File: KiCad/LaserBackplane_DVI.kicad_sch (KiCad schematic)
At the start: 45 parts, among them J1 Curr. Mod., J2 DVI-I, J3 Ld+, J4 Ld-, J5 Pz+, J6 Pz-, J7 Piezo_In, K1 G6AU, Q1 MMBT3904, Q2 2N4401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

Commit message: Add alternative part for inductor.
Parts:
- L1: Alternative (none) -> Coilcraft XAL5050-223MEC
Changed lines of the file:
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@@
+      (effects (font (size 1.27 1.27)) hide)
+    )
+    (property "Alternative" "Coilcraft XAL5050-223MEC" (id 6) (at 173.99 74.93 90)
       (effects (font (size 1.27 1.27)) hide)
     )

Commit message: Update document information
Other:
- company: APQ -> Atoms-Photons-Quanta, Institut für Angewandte Physik, TU Darmstadt
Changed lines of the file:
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@@
     (date "2021-12-16")
     (rev "1.7")
-    (company "APQ")
+    (company "Atoms-Photons-Quanta, Institut für Angewandte Physik, TU Darmstadt")
     (comment 1 "Tilman Preuschoff & Patrick Baus")
   )

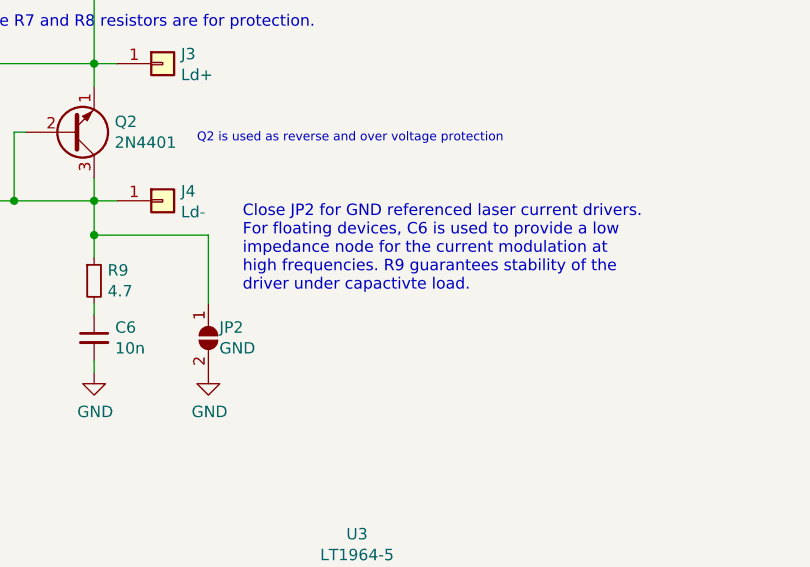
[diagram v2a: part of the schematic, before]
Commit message: Add variants ('default': without current mod., 'curr_mod': with current mod.)
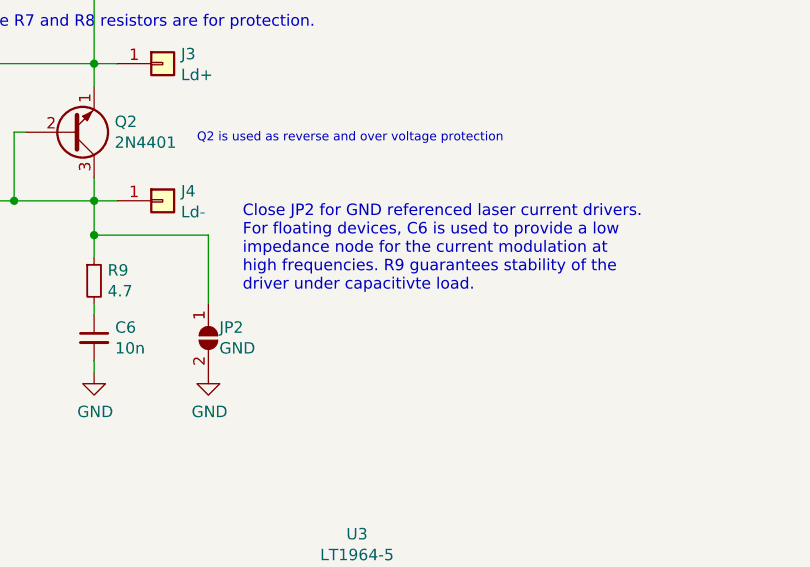
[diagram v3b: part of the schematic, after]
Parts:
- C10, C11, C12, C4, C7, C8, C9, R2, R4, R6, RN1, U1, U2, U3: Config (none) -> +curr_mod
- J1: Config DNF -> +curr_mod; MFN (none) -> Amphenol; PN (none) -> 132291
- J7: Config DNF -> (none); MFN (none) -> Amphenol; PN (none) -> 132291
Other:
- note added: "Close JP2 for GND referenced laser current drivers. For floating devices, C6 is used to provide a low impedance node for the current modulation at high frequencies. R9 guarantees stability of the driver under capacitivte load."
- note removed: "Close JP2 for GND referenced laser current drivers. For floating devices, C6 is used to provide a low impedance node for the current modulation at high frequencies. R9 guarantees stability of the driver under capactivte load."
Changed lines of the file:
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@@
   (title_block
     (title "Laser Backplane Diode DVI")
-    (date "2021-12-16")
-    (rev "1.7")
+    (date "2023-11-02")
+    (rev "1.7.2")
     (company "Atoms-Photons-Quanta, Institut für Angewandte Physik, TU Darmstadt")
     (comment 1 "Tilman Preuschoff & Patrick Baus")
@@
     (effects (font (size 1.524 1.524)) (justify left bottom))
   )
-  (text "Close JP2 for GND referenced laser current drivers. \nFor floating devices, C6 is used to provide a low\nimpedance node for the current modulation at \nhigh frequencies. R9 guarantees stability of the \ndriver under capactivte load."
+  (text "Close JP2 for GND referenced laser current drivers. \nFor floating devices, C6 is used to provide a low\nimpedance node for the current modulation at \nhigh frequencies. R9 guarantees stability of the \ndriver under capacitivte load."
     (at 229.87 107.95 0)
     (effects (font (size 1.27 1.27)) (justify left bottom))
@@
       (effects (font (size 1.27 1.27)) hide)
     )
-    (property "Config" "DNF" (id 4) (at 25.4 161.29 0)
+    (property "Config" "+curr_mod" (id 4) (at 25.4 161.29 0)
+      (effects (font (size 1.27 1.27)) hide)
+    )
+    (property "MFN" "Amphenol" (id 5) (at 25.4 161.29 0)
+      (effects (font (size 1.27 1.27)) hide)
+    )
+    (property "PN" "132291" (id 6) (at 25.4 161.29 0)
       (effects (font (size 1.27 1.27)) hide)
     )
@@
     )
     (property "PN" "RC1210FR-0749R9L" (id 5) (at 34.29 166.37 90)
+      (effects (font (size 1.27 1.27)) hide)
+    )
+    (property "Config" "+curr_mod" (id 6) (at 34.29 166.37 90)
       (effects (font (size 1.27 1.27)) hide)
     )
@@
       (effects (font (size 1.27 1.27)) hide)
     )
-    (property "Config" "DNF" (id 4) (at 257.81 29.21 0)
+    (property "Config" "" (id 4) (at 257.81 29.21 0)
+      (effects (font (size 1.27 1.27)) hide)
+    )
+    (property "MFN" "Amphenol" (id 5) (at 257.81 29.21 0)
+      (effects (font (size 1.27 1.27)) hide)
+    )
+    (property "PN" "132291" (id 6) (at 257.81 29.21 0)
       (effects (font (size 1.27 1.27)) hide)
     )
@@
       (effects (font (size 1.27 1.27)) hide)
     )
+    (property "Config" "+curr_mod" (id 6) (at 171.45 143.51 0)
+      (effects (font (size 1.27 1.27)) hide)
+    )
     (pin "1")
     (pin "2")
@@
       (effects (font (size 1.27 1.27)) hide)
     )
+    (property "Config" "+curr_mod" (id 6) (at 189.23 144.78 0)
+      (effects (font (size 1.27 1.27)) hide)
+    )
     (pin "1")
     (pin "2")
@@
       (effects (font (size 1.27 1.27)) hide)
     )
+    (property "Config" "+curr_mod" (id 6) (at 152.4 144.78 0)
+      (effects (font (size 1.27 1.27)) hide)
+    )
     (pin "1")
     (pin "2")
@@
     )
     (property "PN" "GRM21BR61H475KE51L" (id 5) (at 198.12 144.78 0)
+      (effects (font (size 1.27 1.27)) hide)
+    )
+    (property "Config" "+curr_mod" (id 6) (at 198.12 144.78 0)
       (effects (font (size 1.27 1.27)) hide)
     )
@@
       (effects (font (size 1.27 1.27)) hide)
     )
+    (property "Config" "+curr_mod" (id 6) (at 260.35 144.78 0)
+      (effects (font (size 1.27 1.27)) hide)
+    )
     (pin "1")
     (pin "2")
@@
       (effects (font (size 1.27 1.27)) hide)
     )
+    (property "Config" "+curr_mod" (id 6) (at 223.52 144.78 0)
+      (effects (font (size 1.27 1.27)) hide)
+    )
     (pin "1")
     (pin "2")
@@
     )
     (property "PN" "GRM21BR61H475KE51L" (id 5) (at 269.24 144.78 0)
+      (effects (font (size 1.27 1.27)) hide)
+    )
+    (property "Config" "+curr_mod" (id 6) (at 269.24 144.78 0)
       (effects (font (size 1.27 1.27)) hide)
     )
@@
       (effects (font (size 1.27 1.27)) hide)
     )
+    (property "Config" "+curr_mod" (id 6) (at 242.57 143.51 0)
+      (effects (font (size 1.27 1.27)) hide)
+    )
     (pin "1")
     (pin "2")
@@
       (effects (font (size 1.27 1.27)) hide)
     )
+    (property "Config" "+curr_mod" (id 6) (at 68.58 163.83 0)
+      (effects (font (size 1.27 1.27)) hide)
+    )
     (pin "1")
     (pin "2")
     (pin "3")
+    (pin "5")
+    (pin "6")
+    (pin "7")
+    (pin "4")
+    (pin "8")
   )
   (symbol (lib_id "Amplifier_Operational:ADA4807-2ARM") (at 113.03 166.37 0) (unit 2)
@@
       (effects (font (size 1.27 1.27)) hide)
     )
+    (property "Config" "+curr_mod" (id 6) (at 68.58 163.83 0)
+      (effects (font (size 1.27 1.27)) hide)
+    )
+    (pin "1")
+    (pin "2")
+    (pin "3")
     (pin "5")
     (pin "6")
     (pin "7")
+    (pin "4")
+    (pin "8")
   )
   (symbol (lib_id "Device:R_Pack04_Split") (at 90.17 163.83 270) (unit 1)
@@
       (effects (font (size 1.27 1.27)) hide)
     )
+    (property "Config" "+curr_mod" (id 6) (at 90.17 163.83 90)
+      (effects (font (size 1.27 1.27)) hide)
+    )
     (pin "1")
     (pin "8")
+    (pin "2")
+    (pin "7")
+    (pin "3")
+    (pin "6")
+    (pin "4")
+    (pin "5")
   )
   (symbol (lib_id "Device:R_Pack04_Split") (at 113.03 152.4 90) (mirror x) (unit 3)
@@
       (effects (font (size 1.27 1.27)) hide)
     )
+    (property "Config" "+curr_mod" (id 6) (at 90.17 163.83 90)
+      (effects (font (size 1.27 1.27)) hide)
+    )
+    (pin "1")
+    (pin "8")
+    (pin "2")
+    (pin "7")
     (pin "3")
     (pin "6")
+    (pin "4")
+    (pin "5")
   )
   (symbol (lib_id "Device:R_Pack04_Split") (at 113.03 179.07 90) (mirror x) (unit 4)
@@
       (effects (font (size 1.27 1.27)) hide)
     )
+    (property "Config" "+curr_mod" (id 6) (at 90.17 163.83 90)
+      (effects (font (size 1.27 1.27)) hide)
+    )
+    (pin "1")
+    (pin "8")
+    (pin "2")
+    (pin "7")
+    (pin "3")
+    (pin "6")
     (pin "4")
     (pin "5")
@@
       (effects (font (size 1.27 1.27)) hide)
     )
+    (property "Config" "+curr_mod" (id 6) (at 90.17 163.83 90)
+      (effects (font (size 1.27 1.27)) hide)
+    )
+    (pin "1")
+    (pin "8")
     (pin "2")
     (pin "7")
+    (pin "3")
+    (pin "6")
+    (pin "4")
+    (pin "5")
   )
   (symbol (lib_id "Device:C_Small") (at 113.03 187.96 270) (unit 1)
@@
       (effects (font (size 1.27 1.27)) hide)
     )
+    (property "Config" "+curr_mod" (id 6) (at 113.03 187.96 90)
+      (effects (font (size 1.27 1.27)) hide)
+    )
     (pin "1")
     (pin "2")
@@
       (effects (font (size 1.27 1.27)) hide)
     )
+    (property "Config" "+curr_mod" (id 6) (at 68.58 163.83 0)
+      (effects (font (size 1.27 1.27)) hide)
+    )
+    (pin "1")
+    (pin "2")
+    (pin "3")
+    (pin "5")
+    (pin "6")
+    (pin "7")
     (pin "4")
     (pin "8")
@@
       (effects (font (size 1.27 1.27)) hide)
     )
+    (property "Config" "+curr_mod" (id 6) (at 100.33 147.32 90)
+      (effects (font (size 1.27 1.27)) hide)
+    )
     (pin "1")
     (pin "2")
@@
       (effects (font (size 1.27 1.27)) hide)
     )
+    (property "Config" "+curr_mod" (id 6) (at 43.18 161.29 0)
+      (effects (font (size 1.27 1.27)) hide)
+    )

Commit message: Updated to KiCad 7 Updated footprints
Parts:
- C1, C2: PN C0603C103K2RECAUTO -> C0603C103K2RECAUTO
- D2: footprint Diode_SMD:D_SOT-23_ANK -> Package_TO_SOT_SMD:SOT-23; symbol Device:D_Schottky -> Device:D_Schottky_AKK
- FB1, FB2: MFN Murata -> Murata
- J3: footprint Connector_Wire:SolderWirePad_1x01_Drill1mm -> Connector_Wire:SolderWire-0.5sqmm_1x01_D0.9mm_OD2.3mm
- LOGO1, LOGO2: Config DNF -> (none); now left out of the parts list
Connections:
- net Relay-: now also D2.3 (K); no longer D2.1 (K)
- net at K1.16, Q1.2 (E): now also D2.1 (A); no longer D2.2 (A)
- no-connect marks 21 -> 22
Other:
- note added: "1"
- note added: "3"
- moved on the sheet: R3

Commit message: Fixed variants
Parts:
- C10, C11, C12, C4, C7, C8, C9, J1, R2, R4, R6, RN1, U1, U2, U3: variant (none) -> curr_mod
- J3: Config DNF -> (none); now left out of the parts list
- J4: now left out of the parts list
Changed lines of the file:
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@@
+      (effects (font (size 1.27 1.27)) hide)
+    )
+    (property "variant" "curr_mod" (at 25.4 161.29 0)
       (effects (font (size 1.27 1.27)) hide)
     )
@@
     )
     (property "Config" "+curr_mod" (at 34.29 166.37 90)
+      (effects (font (size 1.27 1.27)) hide)
+    )
+    (property "variant" "curr_mod" (at 34.29 166.37 90)
       (effects (font (size 1.27 1.27)) hide)
     )
@@
   )
   (symbol (lib_id "Connector_Generic:Conn_01x01") (at 220.98 82.55 0) (unit 1)
-    (in_bom yes) (on_board yes) (dnp no)
+    (in_bom no) (on_board yes) (dnp no)
     (property "Reference" "J3" (at 223.012 81.4832 0)
       (effects (font (size 1.27 1.27)) (justify left))
@@
       (effects (font (size 1.27 1.27)) hide)
     )
-    (property "Config" "DNF" (at 220.98 82.55 0)
-      (effects (font (size 1.27 1.27)) hide)
-    )
     (property "MFN" "" (at 220.98 82.55 0)
       (effects (font (size 1.27 1.27)) hide)
@@
   )
   (symbol (lib_id "Connector_Generic:Conn_01x01") (at 220.98 97.79 0) (unit 1)
-    (in_bom yes) (on_board yes) (dnp no)
+    (in_bom no) (on_board yes) (dnp no)
     (property "Reference" "J4" (at 223.012 96.7232 0)
       (effects (font (size 1.27 1.27)) (justify left))
@@
     )
     (property "Config" "DNF" (at 220.98 97.79 0)
+      (effects (font (size 1.27 1.27)) hide)
+    )
+    (property "MFN" "" (at 220.98 97.79 0)
+      (effects (font (size 1.27 1.27)) hide)
+    )
+    (property "PN" "" (at 220.98 97.79 0)
       (effects (font (size 1.27 1.27)) hide)
     )
@@
       (effects (font (size 1.27 1.27)) hide)
     )
+    (property "variant" "curr_mod" (at 171.45 143.51 0)
+      (effects (font (size 1.27 1.27)) hide)
+    )
     (pin "1")
     (pin "2")
@@
       (effects (font (size 1.27 1.27)) hide)
     )
+    (property "variant" "curr_mod" (at 189.23 144.78 0)
+      (effects (font (size 1.27 1.27)) hide)
+    )
     (pin "1")
     (pin "2")
@@
       (effects (font (size 1.27 1.27)) hide)
     )
+    (property "variant" "curr_mod" (at 152.4 144.78 0)
+      (effects (font (size 1.27 1.27)) hide)
+    )
     (pin "1")
     (pin "2")
@@
       (effects (font (size 1.27 1.27)) hide)
     )
+    (property "variant" "curr_mod" (at 198.12 144.78 0)
+      (effects (font (size 1.27 1.27)) hide)
+    )
     (pin "1")
     (pin "2")
@@
       (effects (font (size 1.27 1.27)) hide)
     )
+    (property "variant" "curr_mod" (at 260.35 144.78 0)
+      (effects (font (size 1.27 1.27)) hide)
+    )
     (pin "1")
     (pin "2")
@@
       (effects (font (size 1.27 1.27)) hide)
     )
+    (property "variant" "curr_mod" (at 223.52 144.78 0)
+      (effects (font (size 1.27 1.27)) hide)
+    )
     (pin "1")
     (pin "2")
@@
       (effects (font (size 1.27 1.27)) hide)
     )
+    (property "variant" "curr_mod" (at 269.24 144.78 0)
+      (effects (font (size 1.27 1.27)) hide)
+    )
     (pin "1")
     (pin "2")
@@
     )
     (property "Config" "+curr_mod" (at 242.57 143.51 0)
+      (effects (font (size 1.27 1.27)) hide)
+    )
+    (property "variant" "curr_mod" (at 242.57 143.51 0)
       (effects (font (size 1.27 1.27)) hide)
     )
@@
     )
     (property "Config" "+curr_mod" (at 68.58 163.83 0)
+      (effects (font (size 1.27 1.27)) hide)
+    )
+    (property "variant" "curr_mod" (at 68.58 163.83 0)
       (effects (font (size 1.27 1.27)) hide)
     )
@@
       (effects (font (size 1.27 1.27)) hide)
     )
+    (property "variant" "curr_mod" (at 113.03 166.37 0)
+      (effects (font (size 1.27 1.27)) hide)
+    )
     (pin "1")
     (pin "2")
@@
       (effects (font (size 1.27 1.27)) hide)
     )
+    (property "variant" "curr_mod" (at 90.17 163.83 90)
+      (effects (font (size 1.27 1.27)) hide)
+    )
     (pin "1")
     (pin "8")
@@
       (effects (font (size 1.27 1.27)) hide)
     )
+    (property "variant" "curr_mod" (at 113.03 152.4 90)
+      (effects (font (size 1.27 1.27)) hide)
+    )
     (pin "1")
     (pin "8")
@@
       (effects (font (size 1.27 1.27)) hide)
     )
+    (property "variant" "curr_mod" (at 113.03 179.07 90)
+      (effects (font (size 1.27 1.27)) hide)
+    )
     (pin "1")
     (pin "8")
@@
       (effects (font (size 1.27 1.27)) hide)
     )
+    (property "variant" "curr_mod" (at 90.17 172.72 90)
+      (effects (font (size 1.27 1.27)) hide)
+    )
     (pin "1")
     (pin "8")
@@
       (effects (font (size 1.27 1.27)) hide)
     )
+    (property "variant" "curr_mod" (at 113.03 187.96 90)
+      (effects (font (size 1.27 1.27)) hide)
+    )
     (pin "1")
     (pin "2")
@@
     )
     (property "Config" "+curr_mod" (at 68.58 163.83 0)
+      (effects (font (size 1.27 1.27)) hide)
+    )
+    (property "variant" "curr_mod" (at 147.32 176.53 0)
       (effects (font (size 1.27 1.27)) hide)
     )
@@
       (effects (font (size 1.27 1.27)) hide)
     )
+    (property "variant" "curr_mod" (at 100.33 147.32 90)
+      (effects (font (size 1.27 1.27)) hide)
+    )
     (pin "1")
     (pin "2")
@@
       (effects (font (size 1.27 1.27)) hide)
     )
+    (property "variant" "curr_mod" (at 43.18 161.29 0)
+      (effects (font (size 1.27 1.27)) hide)
+    )

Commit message: Replace DNF by 'exclude from bom' for solder pads and logos.
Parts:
- J4: Config DNF -> (none)
- J5, J6, JP2: Config DNF -> (none); now left out of the parts list
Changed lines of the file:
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@@
   )
   (symbol (lib_id "Connector_Generic:Conn_01x01") (at 232.41 29.21 180) (unit 1)
-    (in_bom yes) (on_board yes) (dnp no)
+    (in_bom no) (on_board yes) (dnp no)
     (property "Reference" "J5" (at 234.4928 23.495 0)
       (effects (font (size 1.27 1.27)))
@@
       (effects (font (size 1.27 1.27)) hide)
     )
-    (property "Config" "DNF" (at 232.41 29.21 0)
+    (property "Config" "" (at 232.41 29.21 0)
       (effects (font (size 1.27 1.27)) hide)
     )
@@
   )
   (symbol (lib_id "Connector_Generic:Conn_01x01") (at 232.41 38.1 180) (unit 1)
-    (in_bom yes) (on_board yes) (dnp no)
+    (in_bom no) (on_board yes) (dnp no)
     (property "Reference" "J6" (at 234.4928 32.385 0)
       (effects (font (size 1.27 1.27)))
@@
       (effects (font (size 1.27 1.27)) hide)
     )
-    (property "Config" "DNF" (at 232.41 38.1 0)
+    (property "Config" "" (at 232.41 38.1 0)
       (effects (font (size 1.27 1.27)) hide)
     )
@@
       (effects (font (size 1.27 1.27)) hide)
     )
-    (property "Config" "DNF" (at 220.98 97.79 0)
+    (property "Config" "" (at 220.98 97.79 0)
       (effects (font (size 1.27 1.27)) hide)
     )
@@
   )
   (symbol (lib_id "Jumper:SolderJumper_2_Open") (at 226.06 113.03 270) (unit 1)
-    (in_bom yes) (on_board yes) (dnp no)
+    (in_bom no) (on_board yes) (dnp no)
     (property "Reference" "JP2" (at 227.2792 111.8616 90)
       (effects (font (size 1.27 1.27)) (justify left))
@@
       (effects (font (size 1.27 1.27)) hide)
     )
-    (property "Config" "DNF" (at 226.06 113.03 90)
-      (effects (font (size 1.27 1.27)) hide)
-    )
+    (property "Config" "" (at 226.06 113.03 90)
+      (effects (font (size 1.27 1.27)) hide)
+    )
